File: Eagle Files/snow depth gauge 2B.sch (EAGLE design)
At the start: 24 parts, among them Q1 MMBT2222A, Q2 MMBT4403LT1SMD, Q3 MMBT2222A, Q4 MMBT2222A, U1 TEENSY 3.1, U2 XBEE-1B1

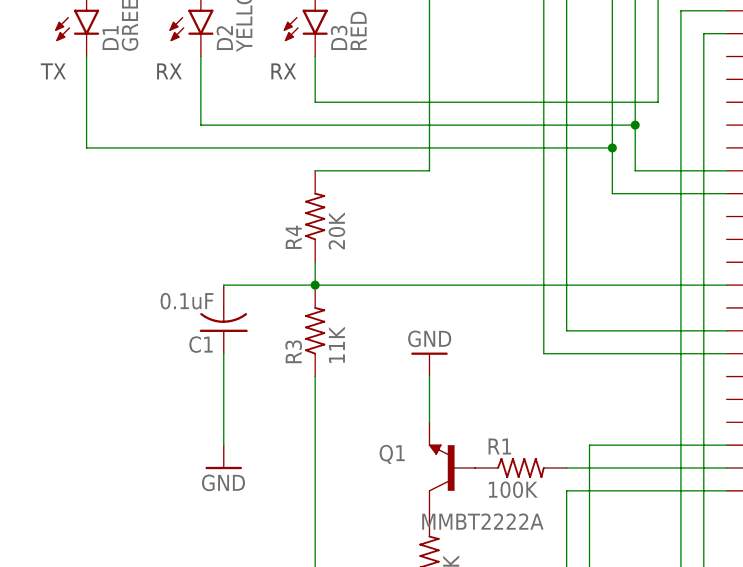
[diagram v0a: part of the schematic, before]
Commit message: PCB Ver. 2B Voltage Divider Update
Updated voltage divider components and values for measuring external 4.2
VDC LiPo battery.
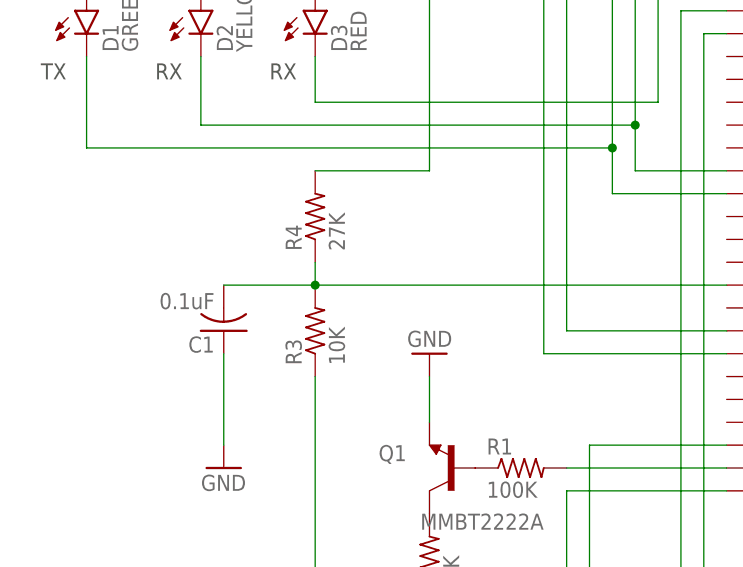
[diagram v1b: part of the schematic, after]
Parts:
- R3: value 11K -> 10K; PARTNO KTR18EZPF1102 -> KTR18EZPJ103
- R4: value 20K -> 27K; PARTNO KTR18EZPF2002 -> KTR18EZPJ273
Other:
- note added: "D C B+G"
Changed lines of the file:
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@@
 <attribute name="PARTNO" value="KTR18EZPJ103"/>
 </part>
-<part name="R4" library="resistor" deviceset="R-US_" device="R3216" value="20K">
-<attribute name="PARTNO" value="KTR18EZPF2002"/>
+<part name="R4" library="resistor" deviceset="R-US_" device="R3216" value="27K">
+<attribute name="PARTNO" value="KTR18EZPJ273"/>
 </part>
 <part name="Q3" library="transistor-neu-to92" deviceset="*-NPN-" device="SOT23-BEC" technology="MMBT2222ALT1" value="MMBT2222A">
@@
 <part name="GND1" library="SparkFun-Aesthetics" deviceset="GND" device=""/>
 <part name="GND4" library="SparkFun-Aesthetics" deviceset="GND" device=""/>
-<part name="R3" library="resistor" deviceset="R-US_" device="R3216" value="11K">
-<attribute name="PARTNO" value="KTR18EZPF1102"/>
+<part name="R3" library="resistor" deviceset="R-US_" device="R3216" value="10K">
+<attribute name="PARTNO" value="KTR18EZPJ103"/>
 </part>
 <part name="U2" library="SparkFun-RF" deviceset="XBEE-1" device="B1">
@@
 <circle x="223.52" y="73.406" radius="0.0254" width="1.27" layer="97"/>
 <wire x1="222.25" y1="79.756" x2="222.25" y2="74.93" width="0.1524" layer="97"/>
+<text x="94.742" y="51.308" size="1.778" layer="150">D C B+G</text>
 </plain>
 <instances>
